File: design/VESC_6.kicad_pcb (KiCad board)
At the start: 4 copper layers, 60 x 60 mm, 305 parts, among them P1 USB_OTG, P10 PH_C, P11 SUPPLY, P12 GND, P2 BATT_-, P2 CAN, P4 HALL_ENC, P5 COM, P6 SERVO, P7 SWD, P8 PH_A, P9 PH_B, Q1 IRF7749, Q2 IRF7749, Q3 IRF7749, Q4 IRF7749, Q5 IRF7749, Q6 IRF7749, U1 STM32F40X_LQFP64, U10 MPU9150, U2 LM3671, U3 DRV8301, U4 TJA1051TK3, U5 AD8418, U6 AD8418, U7 AD8418, U8 NRF24L01P, U9 CONN_U_FL, X1 8m, X2 16M

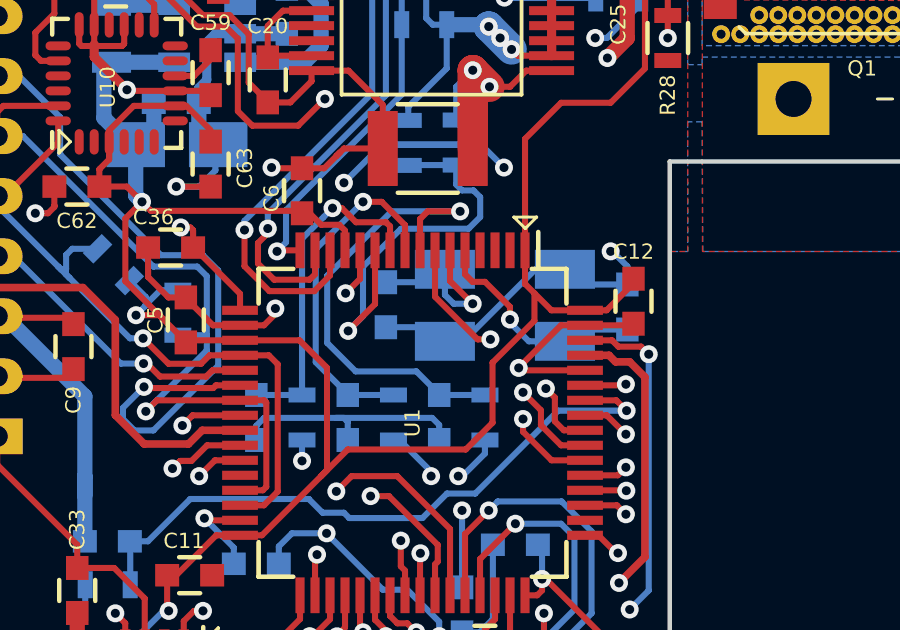
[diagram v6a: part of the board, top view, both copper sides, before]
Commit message: Make Loops Small
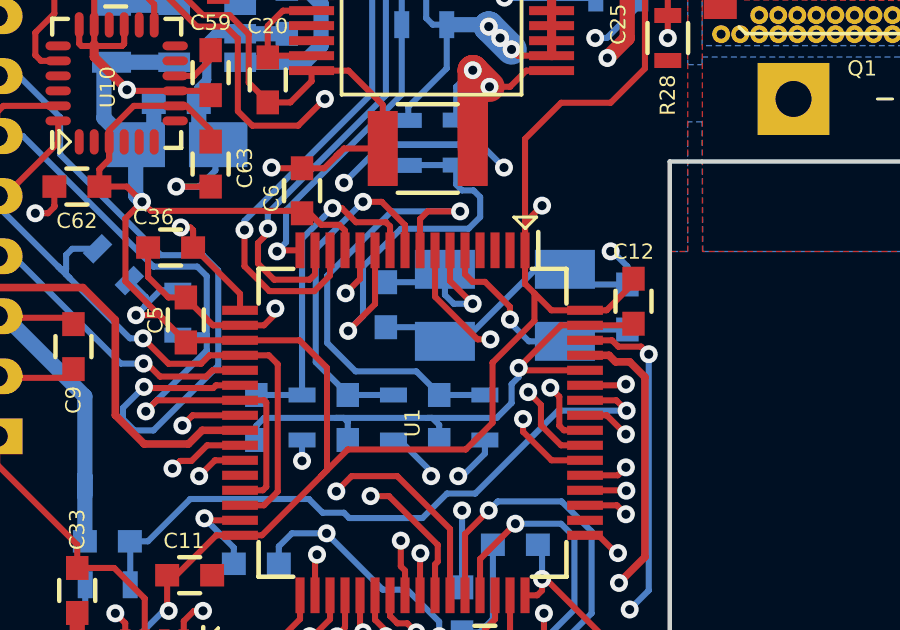
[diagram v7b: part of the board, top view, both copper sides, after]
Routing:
- net GND: track 314.4 -> 318.7 mm
- net VCC: track 215.7 -> 217.4 mm, vias 13 -> 14
- net /nrf/MOSI: track 42.5 -> 41.9 mm
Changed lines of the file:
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@@
     (thickness 1.6)
     (drawings 113)
-    (tracks 2037)
+    (tracks 2048)
     (zones 0)
     (modules 305)
@@
   (segment (start 137.575999 91.959999) (end 138.618409 91.959999) (width 0.2032) (layer F.Cu) (net 1) (status 10))
   (via (at 138.962702 92.304292) (size 0.6) (drill 0.3) (layers F.Cu B.Cu) (net 1))
+  (segment (start 132.334 92.546) (end 134.632402 92.546) (width 0.2032) (layer B.Cu) (net 2))
+  (segment (start 135.128009 91.420486) (end 135.365271 91.183224) (width 0.2032) (layer B.Cu) (net 2))
+  (segment (start 134.632402 92.546) (end 135.128009 92.050393) (width 0.2032) (layer B.Cu) (net 2))
+  (segment (start 132.334 92.546) (end 132.481 92.546) (width 0.2032) (layer B.Cu) (net 2))
+  (segment (start 129.281 92.546) (end 132.334 92.546) (width 0.2032) (layer B.Cu) (net 2))
+  (segment (start 135.128009 92.050393) (end 135.128009 91.420486) (width 0.2032) (layer B.Cu) (net 2))
+  (segment (start 135.365271 91.183224) (end 135.365271 90.87914) (width 0.2032) (layer B.Cu) (net 2))
   (segment (start 139.39 63.586) (end 139.39 62.6578) (width 0.2032) (layer B.Cu) (net 2) (status 10))
   (segment (start 139.39 62.6578) (end 138.9622 62.23) (width 0.2032) (layer B.Cu) (net 2))
@@
   (segment (start 131.191 107.309883) (end 130.307117 107.309883) (width 0.2032) (layer F.Cu) (net 2) (status 30))
   (segment (start 130.307117 107.309883) (end 129.801535 107.815465) (width 0.2032) (layer F.Cu) (net 2) (status 30))
-  (segment (start 129.281 92.546) (end 132.481 92.546) (width 0.2032) (layer B.Cu) (net 2))
   (segment (start 132.481 92.546) (end 132.715 92.78) (width 0.2032) (layer B.Cu) (net 2))
   (segment (start 132.715 92.78) (end 132.715 93.2822) (width 0.2032) (layer B.Cu) (net 2) (status 20))
@@
   (segment (start 135.001 100.0125) (end 135.076001 99.937499) (width 0.2032) (layer F.Cu) (net 5) (status 30))
   (segment (start 135.076001 99.937499) (end 135.076001 98.459999) (width 0.2032) (layer F.Cu) (net 5) (status 30))
+  (segment (start 135.576 86.960001) (end 135.576 86.039) (width 0.2032) (layer F.Cu) (net 6) (status 10))
+  (segment (start 135.576 86.039) (end 136.144 85.471) (width 0.2032) (layer F.Cu) (net 6))
+  (via (at 136.144 85.471) (size 0.6) (drill 0.3) (layers F.Cu B.Cu) (net 6))
   (segment (start 126.1745 63.5875) (end 125.8965 63.5875) (width 0.508) (layer B.Cu) (net 6) (status 30))
   (segment (start 125.8965 63.5875) (end 125.349 64.135) (width 0.508) (layer B.Cu) (net 6) (status 10))
@@
   (segment (start 127.50673 78.97114) (end 127 79.47787) (width 0.2032) (layer F.Cu) (net 16))
   (segment (start 127 79.47787) (end 127 80.542) (width 0.2032) (layer F.Cu) (net 16) (status 20))
-  (segment (start 140.348 63.754) (end 140.323 63.754) (width 0.2032) (layer F.Cu) (net 17))
-  (segment (start 141.097 64.503) (end 140.348 63.754) (width 0.2032) (layer F.Cu) (net 17))
+  (segment (start 140.348 63.754) (end 140.323 63.754) (width 0.2032) (layer F.Cu) (net 17) (status 30))
+  (segment (start 141.097 64.503) (end 140.348 63.754) (width 0.2032) (layer F.Cu) (net 17) (status 20))
   (segment (start 141.097 65.659) (end 141.097 64.503) (width 0.2032) (layer F.Cu) (net 17))
-  (segment (start 136.4615 67.47256) (end 137.06221 67.47256) (width 0.2032) (layer F.Cu) (net 17))
+  (segment (start 136.4615 67.47256) (end 137.06221 67.47256) (width 0.2032) (layer F.Cu) (net 17) (status 30))
   (segment (start 138.413781 66.120989) (end 140.635011 66.120989) (width 0.2032) (layer F.Cu) (net 17))
   (segment (start 140.635011 66.120989) (end 141.097 65.659) (width 0.2032) (layer F.Cu) (net 17))
-  (segment (start 137.06221 67.47256) (end 138.413781 66.120989) (width 0.2032) (layer F.Cu) (net 17))
+  (segment (start 137.06221 67.47256) (end 138.413781 66.120989) (width 0.2032) (layer F.Cu) (net 17) (status 10))
   (segment (start 136.4615 71.47052) (end 137.83748 71.47052) (width 0.2032) (layer F.Cu) (net 18) (status 10))
   (segment (start 137.83748 71.47052) (end 138.303 71.005) (width 0.2032) (layer F.Cu) (net 18) (status 20))
@@
   (segment (start 121.539 85.09) (end 121.539 73.914) (width 0.2032) (layer GND.Cu) (net 82))
   (segment (start 132.460996 93.599) (end 130.048 93.599) (width 0.2032) (layer GND.Cu) (net 82))
-  (segment (start 140.04 67.986) (end 140.04 66.888002) (width 0.2032) (layer B.Cu) (net 82))
-  (segment (start 139.653999 66.502001) (end 139.953998 66.802) (width 0.2032) (layer GND.Cu) (net 82))
-  (segment (start 139.191998 66.04) (end 139.653999 66.502001) (width 0.2032) (layer GND.Cu) (net 82))
+  (segment (start 140.04 67.986) (end 140.04 66.888002) (width 0.2032) (layer B.Cu) (net 82) (status 10))
+  (segment (start 139.191998 66.04) (end 139.953998 66.802) (width 0.2032) (layer GND.Cu) (net 82))
   (segment (start 133.349996 94.488) (end 132.460996 93.599) (width 0.2032) (layer GND.Cu) (net 82))
   (segment (start 140.04 66.888002) (end 139.953998 66.802) (width 0.2032) (layer B.Cu) (net 82))
@@
   (segment (start 137.575999 93.96) (end 136.461748 93.96) (width 0.2032) (layer F.Cu) (net 98) (status 10))
   (via (at 135.509 92.582988) (size 0.6) (drill 0.3) (layers F.Cu B.Cu) (net 98))
-  (segment (start 137.515609 93.751391) (end 137.515609 93.700609) (width 0.2032) (layer PWR.Cu) (net 99))
-  (segment (start 137.515609 93.700609) (end 135.509 91.694) (width 0.2032) (layer PWR.Cu) (net 99))
+  (segment (start 136.105986 92.110383) (end 135.68201 91.686407) (width 0.2032) (layer F.Cu) (net 99))
+  (segment (start 136.105986 92.790088) (end 136.105986 92.110383) (width 0.2032) (layer F.Cu) (net 99))
+  (segment (start 136.775899 93.460001) (end 136.105986 92.790088) (width 0.2032) (layer F.Cu) (net 99))
+  (segment (start 135.68201 91.830174) (end 135.68201 91.686407) (width 0.2032) (layer PWR.Cu) (net 99))
+  (segment (start 137.575999 93.460001) (end 136.775899 93.460001) (width 0.2032) (layer F.Cu) (net 99) (status 10))
+  (segment (start 137.515609 93.663773) (end 135.838468 91.986632) (width 0.2032) (layer PWR.Cu) (net 99))
+  (segment (start 137.541 93.726) (end 137.541 93.689164) (width 0.2032) (layer PWR.Cu) (net 99))
+  (segment (start 137.541 93.689164) (end 135.838468 91.986632) (width 0.2032) (layer PWR.Cu) (net 99))
+  (segment (start 137.515609 93.751391) (end 137.515609 93.663773) (width 0.2032) (layer PWR.Cu) (net 99))
+  (segment (start 135.838468 91.986632) (end 135.68201 91.830174) (width 0.2032) (layer PWR.Cu) (net 99))
+  (via (at 135.68201 91.686407) (size 0.6) (drill 0.3) (layers F.Cu B.Cu) (net 99))
   (segment (start 137.515609 99.471483) (end 137.515609 93.751391) (width 0.2032) (layer PWR.Cu) (net 99))
   (segment (start 137.515609 93.751391) (end 137.541 93.726) (width 0.2032) (layer PWR.Cu) (net 99))
@@
   (segment (start 137.038091 99.943909) (end 137.038091 99.949) (width 0.2032) (layer PWR.Cu) (net 99))
   (segment (start 137.541 99.441) (end 137.541 99.314) (width 0.2032) (layer PWR.Cu) (net 99))
-  (segment (start 135.509 91.694) (end 137.541 93.726) (width 0.2032) (layer PWR.Cu) (net 99))
-  (segment (start 136.105986 92.290986) (end 135.509 91.694) (width 0.2032) (layer F.Cu) (net 99))
-  (segment (start 136.775899 93.460001) (end 136.105986 92.790088) (width 0.2032) (layer F.Cu) (net 99))
-  (segment (start 137.575999 93.460001) (end 136.775899 93.460001) (width 0.2032) (layer F.Cu) (net 99) (status 10))
-  (segment (start 136.105986 92.790088) (end 136.105986 92.290986) (width 0.2032) (layer F.Cu) (net 99))
-  (via (at 135.509 91.694) (size 0.6) (drill 0.3) (layers F.Cu B.Cu) (net 99))
   (segment (start 129.447982 105.390089) (end 128.832893 104.775) (width 0.2032) (layer F.Cu) (net 99) (status 10))
   (segment (start 128.832893 104.775) (end 124.968006 104.775) (width 0.2032) (layer F.Cu) (net 99))
   (via (at 124.968006 104.775) (size 0.6) (drill 0.3) (layers F.Cu B.Cu) (net 99))
+  (segment (start 136.719648 91.838036) (end 136.419649 91.538037) (width 0.2032) (layer F.Cu) (net 100))
+  (segment (start 136.719648 92.810151) (end 136.719648 91.838036) (width 0.2032) (layer F.Cu) (net 100))
+  (via (at 136.419649 91.538037) (size 0.6) (drill 0.3) (layers F.Cu B.Cu) (net 100))
+  (segment (start 136.869497 92.96) (end 136.719648 92.810151) (width 0.2032) (layer F.Cu) (net 100))
+  (segment (start 137.922 93.040388) (end 136.419649 91.538037) (width 0.2032) (layer PWR.Cu) (net 100))
+  (segment (start 137.922 99.695) (end 137.922 93.040388) (width 0.2032) (layer PWR.Cu) (net 100))
   (segment (start 126.817888 103.251) (end 134.366 103.251) (width 0.2032) (layer PWR.Cu) (net 100))
   (segment (start 125.847898 104.22099) (end 126.817888 103.251) (width 0.2032) (layer PWR.Cu) (net 100))
-  (segment (start 137.922 99.695) (end 137.922 93.218) (width 0.2032) (layer PWR.Cu) (net 100))
-  (segment (start 134.366 103.251) (end 137.922 99.695) (width 0.2032) (layer PWR.Cu) (net 100))
-  (segment (start 137.922 93.218) (end 136.271 91.567) (width 0.2032) (layer PWR.Cu) (net 100))
-  (segment (start 136.570999 91.866999) (end 136.271 91.567) (width 0.2032) (layer F.Cu) (net 100))
-  (segment (start 136.570999 92.661502) (end 136.570999 91.866999) (width 0.2032) (layer F.Cu) (net 100))
-  (segment (start 136.869497 92.96) (end 136.570999 92.661502) (width 0.2032) (layer F.Cu) (net 100))
   (segment (start 137.575999 92.96) (end 136.869497 92.96) (width 0.2032) (layer F.Cu) (net 100) (status 10))
-  (via (at 136.271 91.567) (size 0.6) (drill 0.3) (layers F.Cu B.Cu) (net 100))
+  (segment (start 134.366 103.251) (end 137.922 99.695) (width 0.2032) (layer PWR.Cu) (net 100))
   (segment (start 128.98599 104.22099) (end 125.847898 104.22099) (width 0.2032) (layer F.Cu) (net 100))
   (segment (start 129.801535 105.036535) (end 128.98599 104.22099) (width 0.2032) (layer F.Cu) (net 100) (status 10))

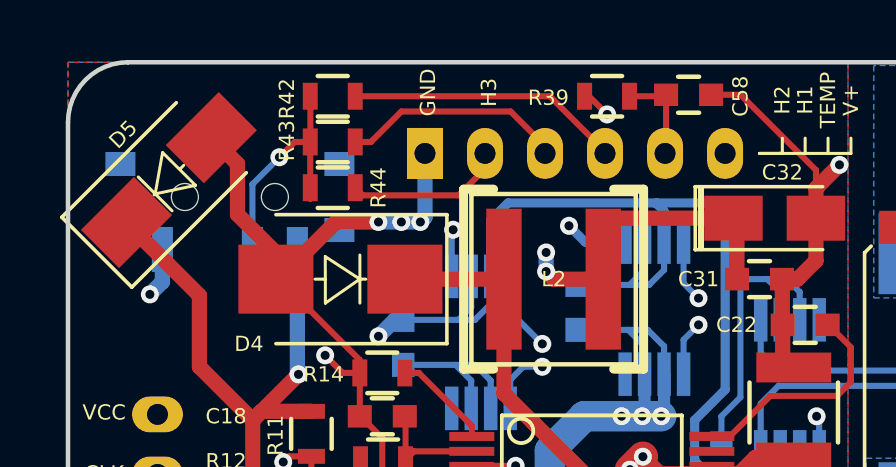
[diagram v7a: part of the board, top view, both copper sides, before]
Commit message: Make Loops Small
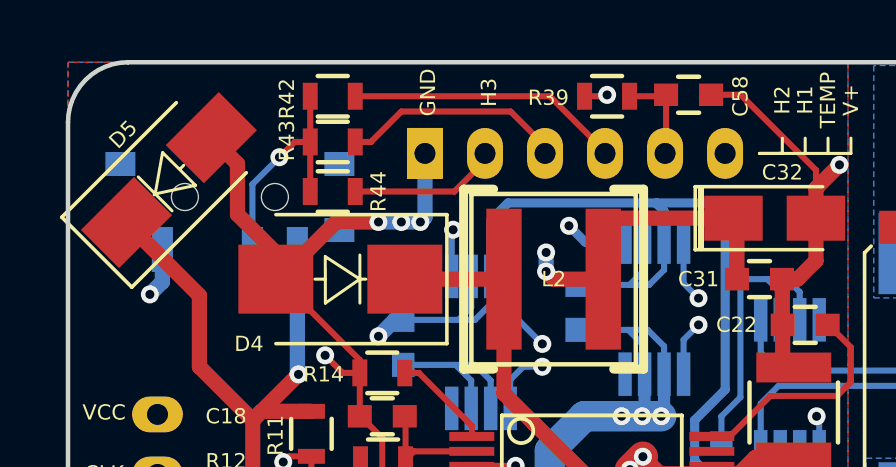
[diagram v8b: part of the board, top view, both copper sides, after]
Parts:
- moved R44 0.13 mm to (123.8, 59.3)
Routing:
- net Net-(P4-Pad6): track 25.2 -> 24.5 mm
- net /MCU/HALL_3: track 69.7 -> 69.1 mm
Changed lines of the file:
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@@
     (thickness 1.6)
     (drawings 113)
-    (tracks 2048)
+    (tracks 2046)
     (zones 0)
     (modules 305)
@@
   )
   (module Resistors_SMD:R_0603 (layer F.Cu)
-    (at 123.825 59.182 180)
+    (at 123.825 59.309 180)
     (descr "Resistor SMD 0603, reflow soldering, Vishay (see dcrcw.pdf)")
     (tags "resistor 0603")
@@
   (segment (start 135.001 100.0125) (end 135.076001 99.937499) (width 0.2032) (layer F.Cu) (net 5) (status 30))
   (segment (start 135.076001 99.937499) (end 135.076001 98.459999) (width 0.2032) (layer F.Cu) (net 5) (status 30))
+  (segment (start 132.924982 56.134) (end 132.970992 56.08799) (width 0.2032) (layer F.Cu) (net 6))
+  (via (at 132.970992 56.08799) (size 0.6) (drill 0.3) (layers F.Cu B.Cu) (net 6))
+  (segment (start 132.219 56.134) (end 132.924982 56.134) (width 0.2032) (layer F.Cu) (net 6) (status 10))
   (segment (start 135.576 86.960001) (end 135.576 86.039) (width 0.2032) (layer F.Cu) (net 6) (status 10))
   (segment (start 135.576 86.039) (end 136.144 85.471) (width 0.2032) (layer F.Cu) (net 6))
@@
   (segment (start 138.74 69.02) (end 138.557 69.203) (width 0.2032) (layer B.Cu) (net 6))
   (segment (start 139.39 68.9142) (end 139.1012 69.203) (width 0.2032) (layer B.Cu) (net 6))
-  (segment (start 132.219 56.134) (end 132.365658 56.134) (width 0.2032) (layer F.Cu) (net 6) (status 30))
-  (segment (start 132.365658 56.134) (end 132.970992 56.739334) (width 0.2032) (layer F.Cu) (net 6) (status 10))
-  (via (at 132.970992 56.739334) (size 0.6) (drill 0.3) (layers F.Cu B.Cu) (net 6))
   (segment (start 118.146 66.5755) (end 117.983 66.7385) (width 0.508) (layer B.Cu) (net 6) (status 30))
   (segment (start 117.983 66.7385) (end 117.0305 66.7385) (width 0.508) (layer GND.Cu) (net 6) (status 10))
@@
   (segment (start 130.90152 57.78881) (end 130.90152 58.039) (width 0.2032) (layer F.Cu) (net 49) (status 30))
   (segment (start 131.09702 57.78881) (end 131.09702 58.039) (width 0.2032) (layer F.Cu) (net 49) (status 30))
-  (segment (start 124.575 59.182) (end 124.829 59.436) (width 0.2032) (layer F.Cu) (net 50) (status 10))
-  (segment (start 124.829 59.436) (end 128.016 59.436) (width 0.2032) (layer F.Cu) (net 50))
-  (segment (start 128.016 59.436) (end 128.9 58.552) (width 0.2032) (layer F.Cu) (net 50) (status 20))
-  (segment (start 128.9 58.552) (end 128.9 58.039) (width 0.2032) (layer F.Cu) (net 50) (status 30))
+  (segment (start 124.575 59.309) (end 127.88019 59.309) (width 0.2032) (layer F.Cu) (net 50) (status 10))
+  (segment (start 127.88019 59.309) (end 128.9 58.28919) (width 0.2032) (layer F.Cu) (net 50) (status 20))
+  (segment (start 128.9 58.28919) (end 128.9 58.039) (width 0.2032) (layer F.Cu) (net 50) (status 30))
   (segment (start 128.9 61.033683) (end 128.9 58.039) (width 0.2032) (layer PWR.Cu) (net 50) (status 20))
   (segment (start 127.652905 62.280778) (end 128.9 61.033683) (width 0.2032) (layer PWR.Cu) (net 50))
@@
   (segment (start 131.075999 99.149707) (end 131.320422 99.39413) (width 0.2032) (layer F.Cu) (net 50))
   (segment (start 131.075999 98.459999) (end 131.075999 99.149707) (width 0.2032) (layer F.Cu) (net 50) (status 10))
-  (segment (start 129.0955 58.039) (end 129.0955 58.28919) (width 0.2032) (layer F.Cu) (net 50) (status 30))
   (segment (start 129.0955 58.039) (end 129.0955 58.2295) (width 0.2032) (layer PWR.Cu) (net 50) (status 30))
   (via (at 131.953 99.695) (size 0.6) (drill 0.3) (layers F.Cu B.Cu) (net 50))
@@
   (segment (start 133.096 57.78881) (end 133.096 58.039) (width 0.2032) (layer F.Cu) (net 51) (status 30))
   (segment (start 133.096 58.28919) (end 133.096 58.039) (width 0.2032) (layer PWR.Cu) (net 51) (status 30))
-  (segment (start 136.90354 56.79067) (end 136.24687 56.134) (width 0.2032) (layer PWR.Cu) (net 52))
-  (segment (start 136.90354 58.039) (end 136.90354 56.79067) (width 0.2032) (layer PWR.Cu) (net 52) (status 10))
-  (segment (start 122.047 58.166) (end 122.555 57.658) (width 0.2032) (layer F.Cu) (net 52))
-  (segment (start 122.555 57.658) (end 123.075 57.658) (width 0.2032) (layer F.Cu) (net 52) (status 20))
-  (segment (start 125.603 56.134) (end 123.571 58.166) (width 0.2032) (layer PWR.Cu) (net 52))
+  (segment (start 123.075 57.658) (end 122.555 57.658) (width 0.2032) (layer F.Cu) (net 52) (status 10))
+  (segment (start 122.555 57.658) (end 122.047 58.166) (width 0.2032) (layer F.Cu) (net 52))
+  (segment (start 123.075 57.658) (end 123.075 59.309) (width 0.2032) (layer F.Cu) (net 52) (status 30))
+  (segment (start 123.075 56.134) (end 123.075 57.658) (width 0.2032) (layer F.Cu) (net 52) (status 30))
+  (segment (start 136.90354 58.039) (end 136.90354 57.02054) (width 0.2032) (layer PWR.Cu) (net 52) (status 10))
+  (segment (start 136.90354 57.02054) (end 136.525 56.642) (width 0.2032) (layer PWR.Cu) (net 52))
+  (segment (start 136.525 56.642) (end 125.095 56.642) (width 0.2032) (layer PWR.Cu) (net 52))
+  (segment (start 125.095 56.642) (end 123.571 58.166) (width 0.2032) (layer PWR.Cu) (net 52))
   (segment (start 123.571 58.166) (end 122.047 58.166) (width 0.2032) (layer PWR.Cu) (net 52))
-  (segment (start 136.24687 56.134) (end 125.603 56.134) (width 0.2032) (layer PWR.Cu) (net 52))
   (segment (start 122.047 58.166) (end 121.146 59.067) (width 0.2032) (layer B.Cu) (net 52))
   (segment (start 121.146 59.067) (end 121.146 61.247) (width 0.2032) (layer B.Cu) (net 52) (status 20))
   (via (at 122.047 58.166) (size 0.6) (drill 0.3) (layers F.Cu B.Cu) (net 52))
-  (segment (start 123.075 57.912) (end 123.075 59.563) (width 0.2032) (layer F.Cu) (net 52) (status 30))
-  (segment (start 123.0793 56.3057) (end 123.0793 57.9077) (width 0.2032) (layer F.Cu) (net 52) (status 30))
   (segment (start 123.0793 57.9077) (end 123.075 57.912) (width 0.2032) (layer F.Cu) (net 52) (status 30))
   (segment (start 120.0785 83.761592) (end 120.0785 82.52245) (width 0.2032) (layer B.Cu) (net 53))
